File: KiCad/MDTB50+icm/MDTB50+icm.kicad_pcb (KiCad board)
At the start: 2 copper layers, 15.2 x 31.5 mm, 23 parts, among them U1 ICM-45686

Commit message: - DIY PCB fully routed. But it kinda sucks.
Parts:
- renumbered U3 to TP1
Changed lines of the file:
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@@
 		(descr "Paw-Tag-Connect programming header; http://www.tag-connect.com/Materials/TC2030-IDC-NL.pdf; https://github.com/LeoDJ/Paw-Connect")
 		(tags "paw tag connect programming header pogo pins")
-		(property "Reference" "U3"
+		(property "Reference" "TP1"
 			(at 0.02 -3.01 0)
 			(layer "B.SilkS")
@@
 	)
 	(segment
-		(start 115.310728 78.80011)
-		(end 114.898292 78.80011)
+		(start 114.367642 79.307358)
+		(end 114.367642 80.036645)
 		(width 0.25)
 		(layer "F.Cu")
@@
 	)
 	(segment
-		(start 115.465 78.645838)
-		(end 115.310728 78.80011)
+		(start 115.465 78.21)
+		(end 114.367642 79.307358)
 		(width 0.25)
 		(layer "F.Cu")
@@
 	)
 	(segment
-		(start 114.388482 80.661482)
+		(start 115.515 81.184003)
 		(end 115.515 81.788)
 		(width 0.25)
@@
 	(segment
 		(start 115.465 77.2)
-		(end 115.465 78.645838)
+		(end 115.465 78.21)
 		(width 0.25)
 		(layer "F.Cu")
@@
 	)
 	(segment
-		(start 114.898292 78.80011)
-		(end 114.388482 79.30992)
-		(width 0.25)
-		(layer "F.Cu")
-		(net 6)
-	)
-	(segment
-		(start 114.388482 79.30992)
-		(end 114.388482 80.661482)
+		(start 114.367642 80.036645)
+		(end 115.515 81.184003)
 		(width 0.25)
 		(layer "F.Cu")
@@
 	)
 	(segment
-		(start 112.241317 71.201995)
-		(end 112.37214 71.071172)
-		(width 0.2)
-		(layer "F.Cu")
-		(net 9)
-	)
-	(segment
-		(start 112.37214 74.760471)
-		(end 112.37214 71.829876)
-		(width 0.2)
-		(layer "F.Cu")
-		(net 9)
-	)
-	(segment
-		(start 112.37214 71.829876)
-		(end 112.241317 71.699053)
-		(width 0.2)
-		(layer "F.Cu")
-		(net 9)
-	)
-	(segment
-		(start 114.725 77.56)
-		(end 114.4086 77.8764)
+		(start 111.5726 70.323)
+		(end 110.966 69.7164)
 		(width 0.2)
 		(layer "F.Cu")
@@
 	)
 	(segment
-		(start 112.37214 71.071172)
+		(start 112.37214 74.760471)
 		(end 112.37214 70.323)
 		(width 0.2)
@@
 	)
 	(segment
-		(start 122.206 69.818)
-		(end 122.206 69.218401)
-		(width 0.25)
-		(layer "F.Cu")
-		(net 9)
-	)
-	(segment
-		(start 112.2214 77.8764)
-		(end 112.145 77.8)
+		(start 114.725 77.2)
+		(end 114.725 77.56)
 		(width 0.2)
 		(layer "F.Cu")
@@
 	)
 	(segment
-		(start 112.145 77.8)
-		(end 112.145 74.987611)
+		(start 112.145 74.987611)
+		(end 112.37214 74.760471)
 		(width 0.2)
 		(layer "F.Cu")
@@
 	)
 	(segment
-		(start 112.145 74.987611)
-		(end 112.37214 74.760471)
-		(width 0.2)
+		(start 122.206 69.818)
+		(end 122.206 69.218401)
+		(width 0.25)
 		(layer "F.Cu")
 		(net 9)
 	)
 	(segment
-		(start 111.5726 70.323)
-		(end 110.966 69.7164)
+		(start 110.966 69.7164)
+		(end 110.966 69.218401)
 		(width 0.2)
 		(layer "F.Cu")
@@
 	)
 	(segment
-		(start 114.4086 77.8764)
-		(end 112.2214 77.8764)
+		(start 114.725 77.56)
+		(end 114.4086 77.8764)
 		(width 0.2)
 		(layer "F.Cu")
@@
 	)
 	(segment
-		(start 112.241317 71.699053)
-		(end 112.241317 71.201995)
+		(start 112.2214 77.8764)
+		(end 112.145 77.8)
 		(width 0.2)
 		(layer "F.Cu")
@@
 	)
 	(segment
-		(start 114.725 77.2)
-		(end 114.725 77.56)
+		(start 114.4086 77.8764)
+		(end 112.2214 77.8764)
 		(width 0.2)
 		(layer "F.Cu")
@@
 	)
 	(segment
-		(start 110.966 69.7164)
-		(end 110.966 69.218401)
+		(start 112.145 77.8)
+		(end 112.145 74.987611)
 		(width 0.2)
 		(layer "F.Cu")
@@
 	)
 	(segment
-		(start 113.12632 71.16552)
-		(end 112.841317 71.450524)
-		(width 0.25)
-		(layer "F.Cu")
-		(net 34)
-	)
-	(segment
 		(start 120.773 87.884)
 		(end 120.7516 87.884)
@@
 	)
 	(segment
-		(start 112.841317 71.450524)
-		(end 112.796828 71.495013)
+		(start 113.035207 71.451806)
+		(end 112.796828 71.690185)
 		(width 0.25)
 		(layer "F.Cu")
@@
 	)
 	(segment
-		(start 112.796828 71.495013)
-		(end 112.796828 71.98276)
-		(width 0.25)
-		(layer "F.Cu")
-		(net 34)
-	)
-	(segment
 		(start 117.692851 87.16)
 		(end 118.289851 87.757)
@@
 	)
 	(segment
+		(start 113.035207 71.256633)
+		(end 113.035207 71.451806)
+		(width 0.25)
+		(layer "F.Cu")
+		(net 34)
+	)
+	(segment
 		(start 114.583694 90.268498)
 		(end 114.583694 90.504494)
@@
 	)
 	(segment
+		(start 113.12632 71.16552)
+		(end 113.035207 71.256633)
+		(width 0.25)
+		(layer "F.Cu")
+		(net 34)
+	)
+	(segment
 		(start 118.3132 87.780349)
 		(end 118.277973 87.815576)
@@
 	)
 	(segment
+		(start 112.796828 71.690185)
+		(end 112.796828 71.98276)
+		(width 0.25)
+		(layer "F.Cu")
+		(net 34)
+	)
+	(segment
 		(start 118.2034 89.5604)
 		(end 118.11 89.467)
@@
 	)
 	(via
-		(at 112.841317 71.450524)
+		(at 113.035207 71.451806)
 		(size 0.6)
 		(drill 0.3)

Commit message: - Changed PCB to 4 layer - Added QMC6309 magnetometer
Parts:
- added C1m1: 2.2uF, passive_custom:C_0402_JLC, F.Cu at (122.8, 75.4)
- added U3: ~, mag_custom:QMC6309, F.Cu at (122.8, 74.2)
- moved U1 1.96 mm to (119.4, 74.5)
- moved C1i1 1.73 mm to (117.1, 73.4), turned to -90 degrees
- moved C2i1 1.42 mm to (121.4, 71.9)
- moved U4 0.57 mm to (114.6, 74.7)
- moved R1U1 0.09 mm to (118.8, 71.9), turned to 0 degrees
- moved R2C1 0.08 mm to (114.4, 85.6)
- moved U2 0.05 mm to (116.5, 67.8)
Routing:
- net +3.3V: track 30.2 -> 18.3 mm, vias 2 -> 6
- net GND: track 86.2 -> 78.5 mm, vias 30 -> 29
- net SDX: track 0.59 -> 6.88 mm, vias 0 -> 2
- net INT1: track 9.54 -> 13.8 mm, vias 0 -> 2
- net VBUS: track 42.3 -> 45.2 mm
- net SCL: track 4.54 -> 2.05 mm
- net SDA: track 4.40 -> 1.96 mm
- net CS: track 5.37 -> 3.11 mm
- net SCX: track 0.59 -> 2.03 mm
- net CLK: track 4.34 -> 3.01 mm
- net USB_CHASSIS: track 17.9 -> 16.7 mm, vias 0 -> 2
- net SDO: track 6.74 -> 7.00 mm, vias 0 -> 2
- added copper zone on In2.Cu, net +3.3V
- added copper zone on In1.Cu, net GND
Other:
- copper layers 2 -> 4
- board text removed: "5k1"

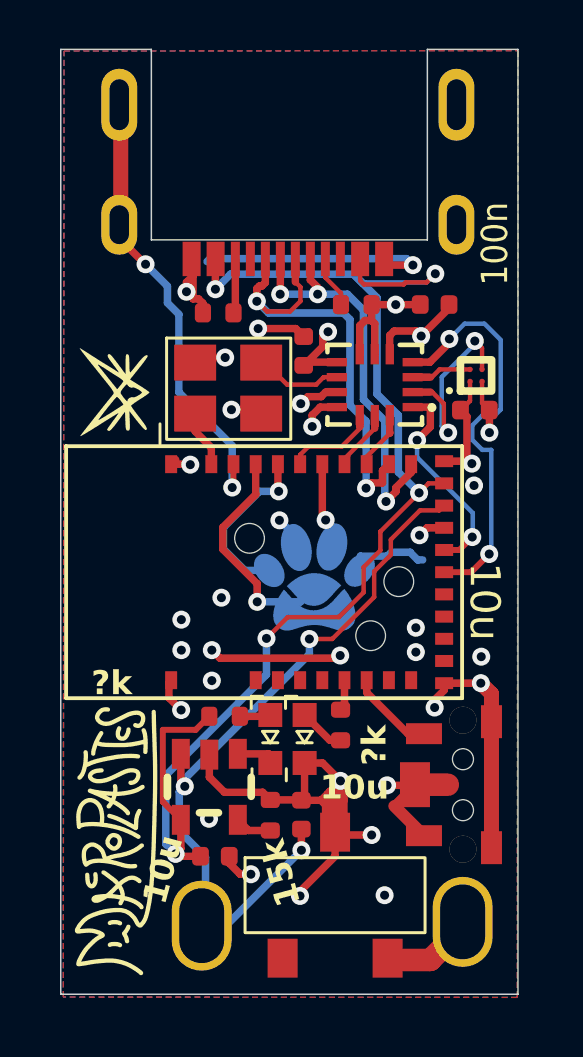
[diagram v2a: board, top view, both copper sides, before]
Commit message: - Finished back silkscreen for high volume version
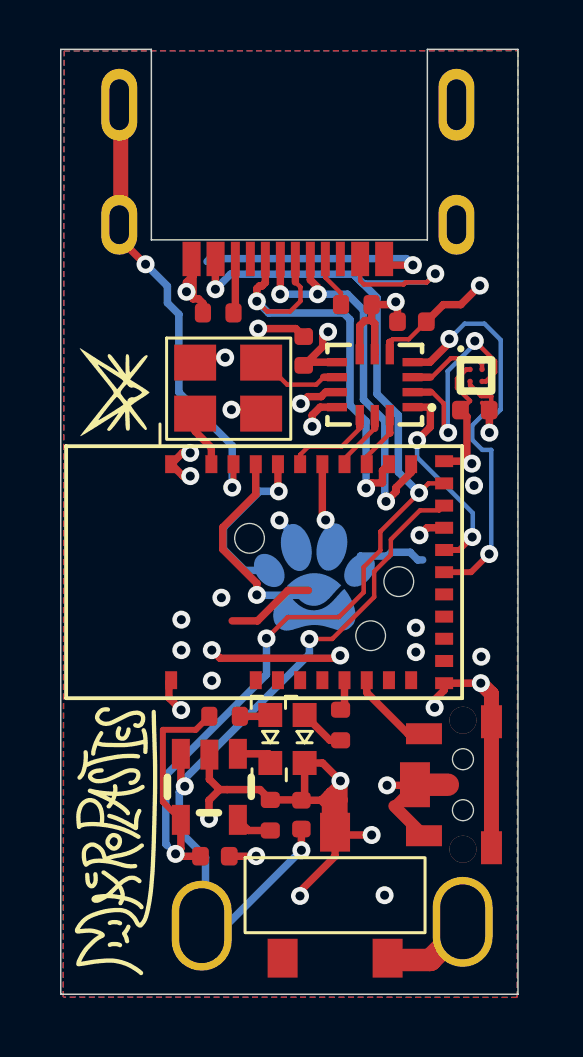
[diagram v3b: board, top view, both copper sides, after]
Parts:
- added G***: LOGO, LOGO, B.Cu at (116.5, 79.2)
- moved C2i1 0.95 mm to (120.7, 72.5)
- turned U3 to 0 degrees
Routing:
- net GND: track 78.5 -> 84.0 mm, vias 29 -> 30
- net +3.3V: track 18.3 -> 21.5 mm
- net SCX: track 2.03 -> 2.84 mm
- net SDX: track 6.88 -> 7.55 mm
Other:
- board text removed: "100n"
- board text removed: "10u"
- board text removed: "15k"
- board text removed: "3V3"
- board text removed: "?k"
- board text removed: "GND"
- board text removed: "RST"
- board text removed: "SWCLK"
- board text removed: "SWDIO"

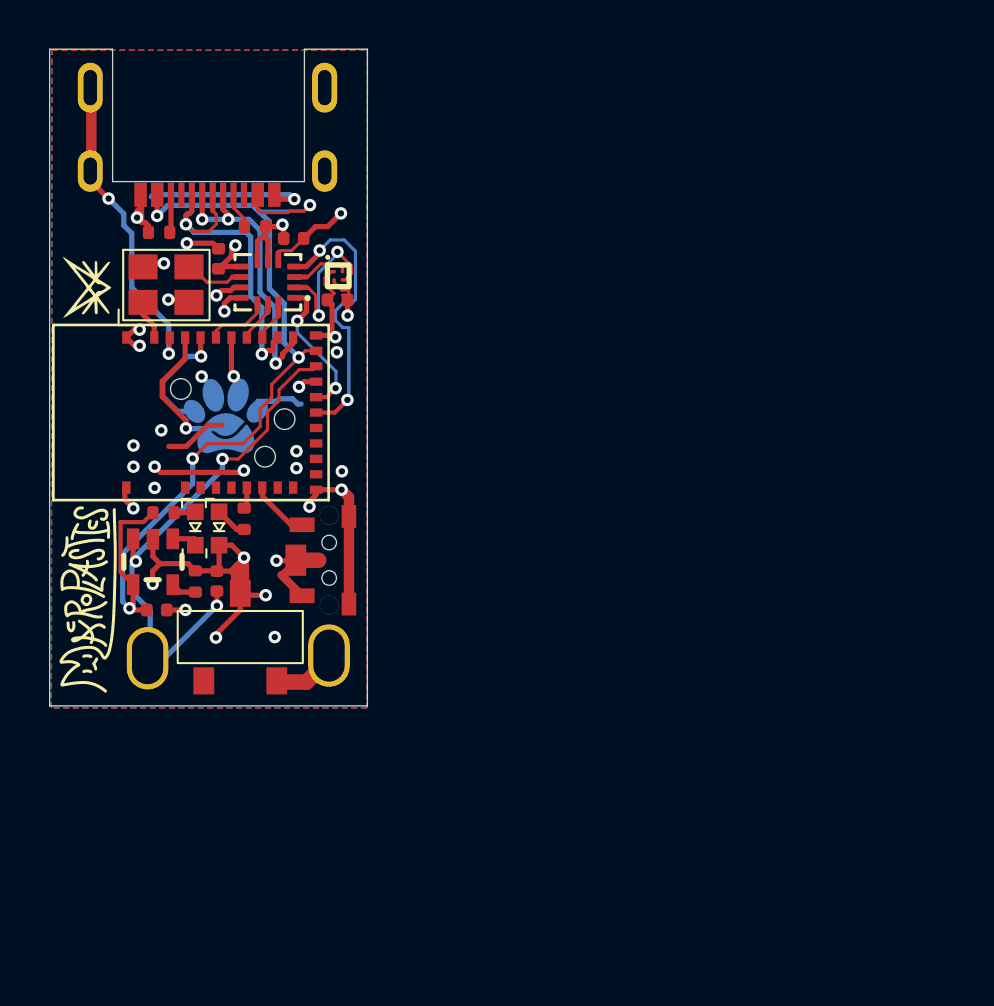
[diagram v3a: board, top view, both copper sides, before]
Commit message: - Added external 1.8v regulator, external 3.3v regulator, QMC6309, logic   level shifter for QMC6309, pushbutton power disconnect - Replaced USB C port for better one
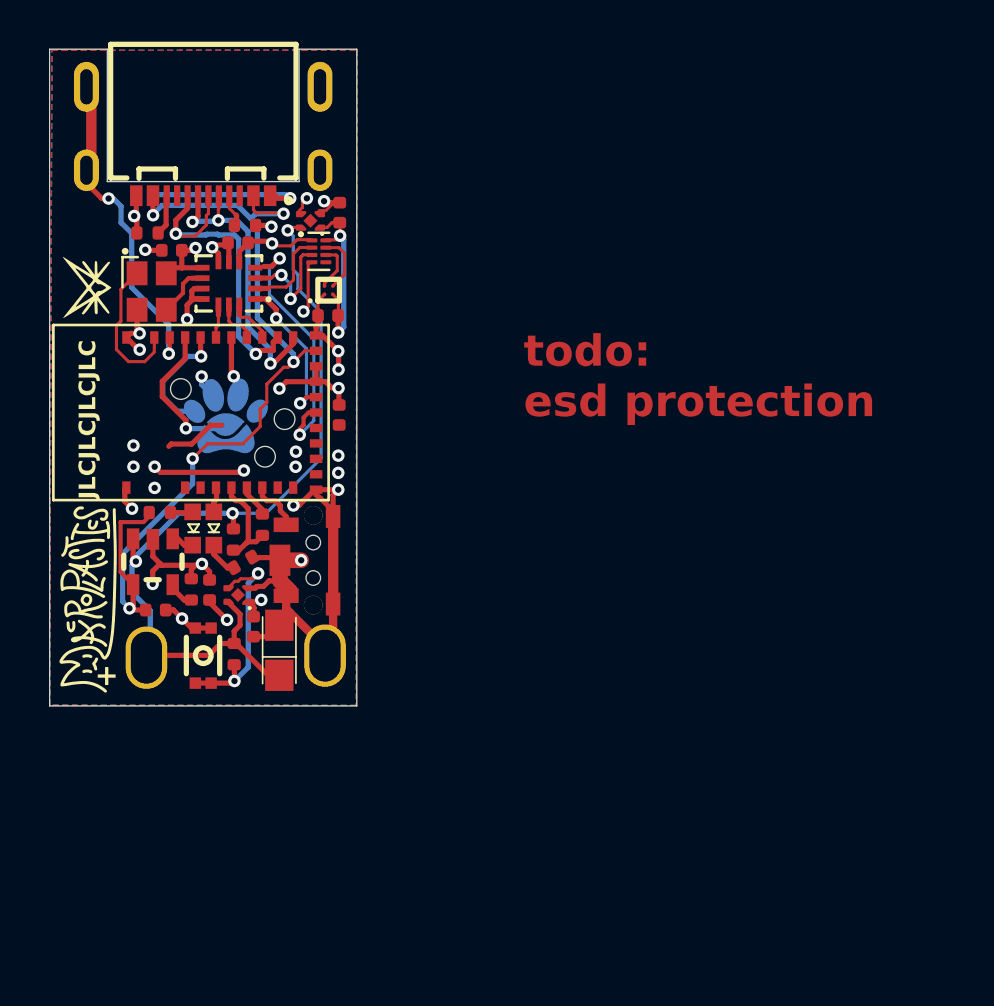
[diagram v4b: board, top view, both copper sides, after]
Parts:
- removed C1C2: 10uF, passive_custom:C_0402_JLC
- added C1: TAJA105K016RNJ, easyeda2kicad:CASE-A_3216, F.Cu at (120.0, 92.2)
- added C1C1: 10uF, passive_custom:C_0402_JLC, F.Cu at (114.1, 90.3)
- added C2R1: 1uF, passive_custom:C_0402_JLC, F.Cu at (118.7, 91.1)
- added C2n1: 10uF, passive_custom:C_0402_JLC, F.Cu at (122.8, 80.9)
- added R1C2: 15k, passive_custom:R_0402_JLC, F.Cu at (117.8, 92.4)
- added R1D1: 100k, passive_custom:R_0402_JLC, F.Cu at (117.8, 86.9)
- added R2D1: 51k, passive_custom:R_0402_JLC, F.Cu at (119.2, 86.2)
- added SW1: 1TS026A-1100-0550-CT, easyeda2kicad:SW-SMD_4P-L2.6-W1.6-P0.75-LS3.0, F.Cu at (116.3, 92.5)
- added USB1: TYPE-C 16P CB0.8 073, easyeda2kicad:USB-C-SMD_TYPE-C-16P-CB0.8-073, F.Cu at (116.3, 67.8)
- added X1: ~, Crystal:Crystal_SMD_2520-4Pin_2.5x2.0mm, F.Cu at (113.9, 75.0)
- added c2_3r1: 1uF, passive_custom:C_0402_JLC, F.Cu at (122.9, 71.2)
- U2: value ~ -> TXS0102DQER; footprint USB-C_Custom:HCTL HC-TYPE-C-16P-CB1.0 -> Package_SON:X2SON-8_1.4x1mm_P0.35mm
- U4: value ~ -> SSP7615-18DFR; footprint oscillator_custom:HCI 1532H4-32K768JWPDTSNL -> easyeda2kicad:DFN-4_L1.0-W1.0-P0.65-BL-EP
- U5: value ~ -> SSP7615-33DFR; footprint Switch_Custom:CJS-1200TB -> easyeda2kicad:DFN-4_L1.0-W1.0-P0.65-BL-EP
- moved U5 20.2 mm to (121.5, 71.6), turned to 90 degrees
- moved U4 15.3 mm to (118.0, 89.5), turned to 90 degrees
- moved U2 7.51 mm to (121.9, 73.1), turned to 0 degrees
- moved C2i1 2.68 mm to (118.0, 72.7)
- moved C1i1 2.29 mm to (114.8, 73.0), turned to 0 degrees
- moved R1n1 2.09 mm to (118.2, 88.0), turned to -150 degrees
- moved U1 1.87 mm to (117.6, 74.6)
- moved C1m1 0.88 mm to (122.3, 76.2)
- moved U3 0.83 mm to (122.3, 74.9), turned to 90 degrees
- moved S1 0.76 mm to (121.3, 87.9)
- moved R2U1 0.56 mm to (113.7, 72.2)
- moved C1n1 0.55 mm to (116.6, 89.3)
- moved R1U1 0.49 mm to (118.3, 71.8)
- moved R1C1 0.43 mm to (115.8, 89.3)
- moved LED1n1 0.25 mm to (116.8, 86.4)
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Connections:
- B-1 pad 1: Net-(B-1-Pad1) -> GND
- C1i1 pad 2: +3.3V -> +1.8V
- C1n1 pad 1: B+ -> +1.8V
- C2i1 pad 2: +3.3V -> +1.8V
- LED1n1 pad 1: GND -> Net-(LED1n1-K)
- MDBT50_1 pad 17: +3.3V -> +1.8V
- MDBT50_1 pad 18: B+ -> +1.8V
- MDBT50_1 pad 4: unconnected-(MDBT50_1-P0.28-Pad4) -> Net-(LED1n1-A)
- MDBT50_1 pad 5: unconnected-(MDBT50_1-P0.29-Pad5) -> ADC
- MDBT50_1 pad 6: Net-(MDBT50_1-P0.30) -> ADC_EN
- R1U1 pad 1: Net-(U2-CC1) -> Net-(USB1-CC1)
- R1n1 pad 1: Net-(MDBT50_1-P0.30) -> GND
- R1n1 pad 2: Net-(LED1n1-A) -> Net-(LED1n1-K)
- R2U1 pad 2: Net-(U2-CC2) -> Net-(USB1-CC2)
- TP1 pad 1: +3.3V -> +1.8V
- TP1 pad 6: SWCLK -> unconnected-(TP1-NC-Pad6)
- U1 pad 2: SDX -> SDX_1v8
- U1 pad 3: SCX -> SCX_1v8
- U1 pad 5: +3.3V -> +1.8V
- U1 pad 8: +3.3V -> +1.8V
- U3 pad A2: SCX -> SCX_3v3
- U3 pad B2: SDX -> SDX_3v3
- U4 pad 1: CLK_EN -> +1.8V
- U4 pad 3: CLK -> Net-(U4-EN)
- U4 pad 4: +3.3V -> B+
- U5 pad 1: unconnected-(U5-Pad1) -> +3.3V
- U5 pad 3: Net-(B-1-Pad1) -> +1.8V
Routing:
- net +1.8V: track 0.00 -> 36.3 mm, vias 0 -> 8
- net B+: track 24.8 -> 39.8 mm
- net +3.3V: track 21.5 -> 9.20 mm, vias 6 -> 2
- net Net-(U4-EN): track 0.00 -> 10.2 mm, vias 0 -> 2
- net SDX: track 7.55 -> 0.00 mm, vias 2 -> 0
- net SCX_1v8: track 0.00 -> 5.43 mm, vias 0 -> 2
- net CLK_EN: track 2.08 -> 7.01 mm
- net ADC: track 0.00 -> 4.84 mm
- net SDX_1v8: track 0.00 -> 4.17 mm
- net Net-(B-1-Pad1): track 3.24 -> 0.00 mm
- net SCX: track 2.84 -> 0.00 mm
- net GND: track 84.0 -> 86.8 mm, vias 30 -> 28
- net SDX_3v3: track 0.00 -> 2.81 mm
- net VBUS: track 45.2 -> 42.6 mm
- net SCX_3v3: track 0.00 -> 2.25 mm
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- added copper zone on In2.Cu, net +1.8V
- removed copper zone on In2.Cu, net +3.3V
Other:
- board size 15.2 x 31.5 mm -> 14.7 x 31.5 mm
- board text added: "+"
- board text added: "JLCJLCJLCJLC"
- board text added: "todo: esd protection"

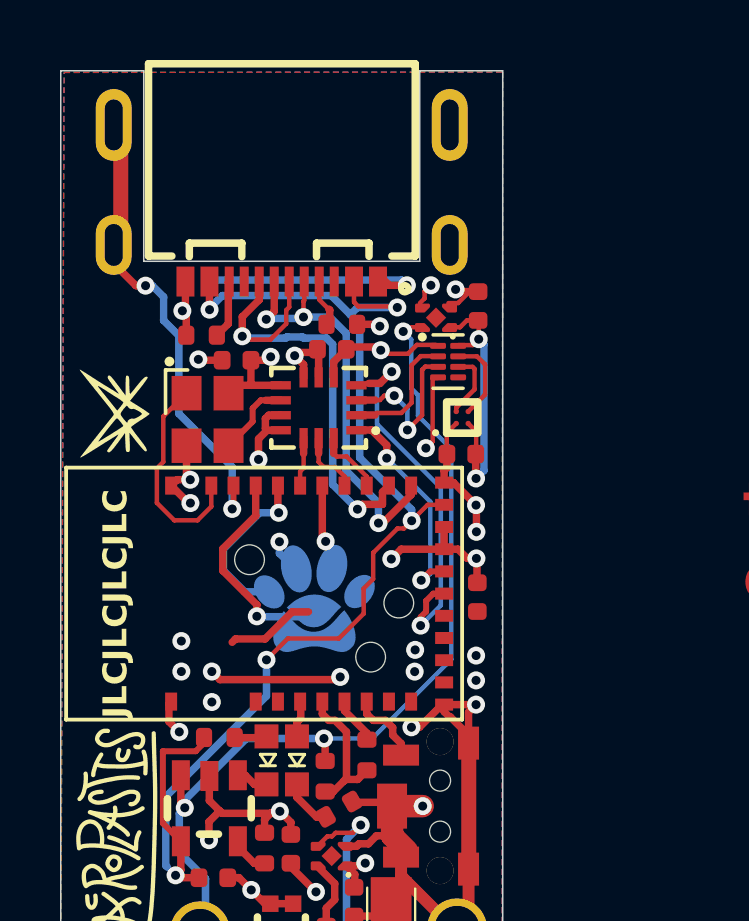
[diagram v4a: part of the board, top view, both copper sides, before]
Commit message: - Added ESD protection
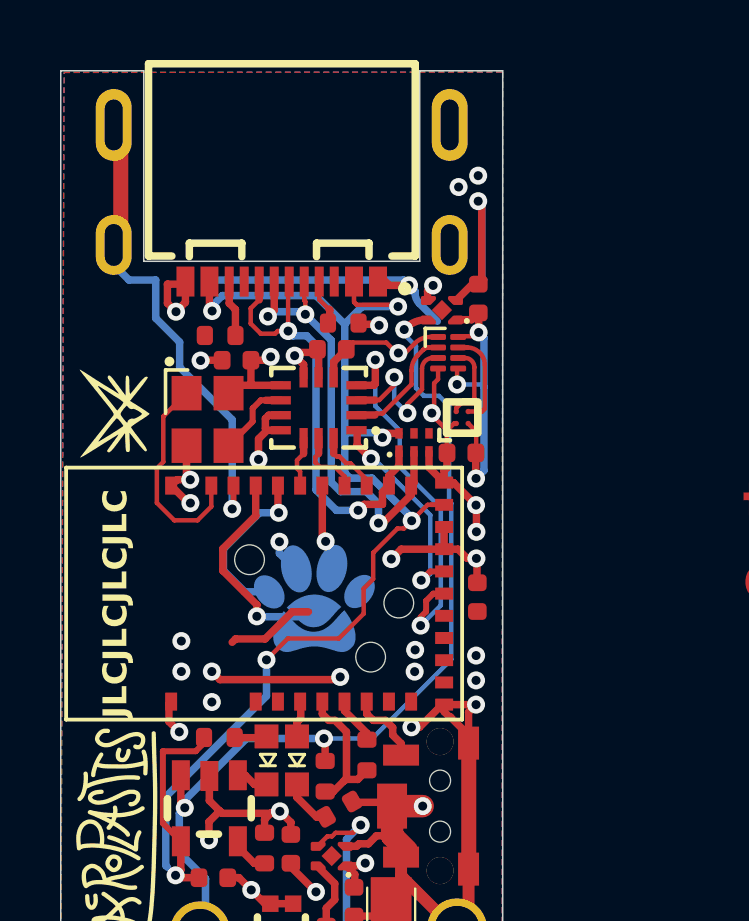
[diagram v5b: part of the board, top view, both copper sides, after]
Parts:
- added D1: TPD3E001DRYR, easyeda2kicad:SON-6_L1.5-W1.0-P0.50-BL_SN74LVC1G19DRYR, F.Cu at (120.7, 75.8)
- moved R2U1 0.62 mm to (114.3, 72.2)
- moved U5 0.32 mm to (121.7, 71.3)
- moved U2 0.30 mm to (121.9, 72.8)
- moved c2_3r1 0.25 mm to (122.9, 70.9)
- moved R1U1 0.06 mm to (118.4, 71.8)
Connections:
- TP1 pad 6: unconnected-(TP1-NC-Pad6) -> SWCLK
- U2 pad 5: MAG_EN -> +3.3V
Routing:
- net GND: track 86.8 -> 97.6 mm, vias 28 -> 30
- net VBUS: track 42.6 -> 45.5 mm, vias 5 -> 6
- net +3.3V: track 9.20 -> 10.7 mm, vias 2 -> 3
- net D-: track 13.9 -> 15.0 mm
- net USB_CHASSIS: track 17.0 -> 18.1 mm, vias 2 -> 1
- net INT1: track 12.4 -> 13.1 mm
- net D+: track 15.9 -> 15.2 mm
- net +1.8V: track 36.3 -> 37.1 mm
- net B+: track 39.8 -> 40.5 mm

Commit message: - No more non 90deg angles on components. Yay.
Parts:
- moved R1n1 0.53 mm to (117.7, 88.2), turned to 180 degrees
- moved C1n1 0.13 mm to (116.6, 89.5)
- moved R1C1 0.13 mm to (115.7, 89.4)
- moved R2D1 0.09 mm to (119.1, 86.2)
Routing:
- net GND: track 97.6 -> 98.7 mm
- net USB_CHASSIS: track 18.1 -> 17.5 mm
